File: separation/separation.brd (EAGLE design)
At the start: 71.1 x 26.7 mm, 9 parts, among them IC1 L7805ACV

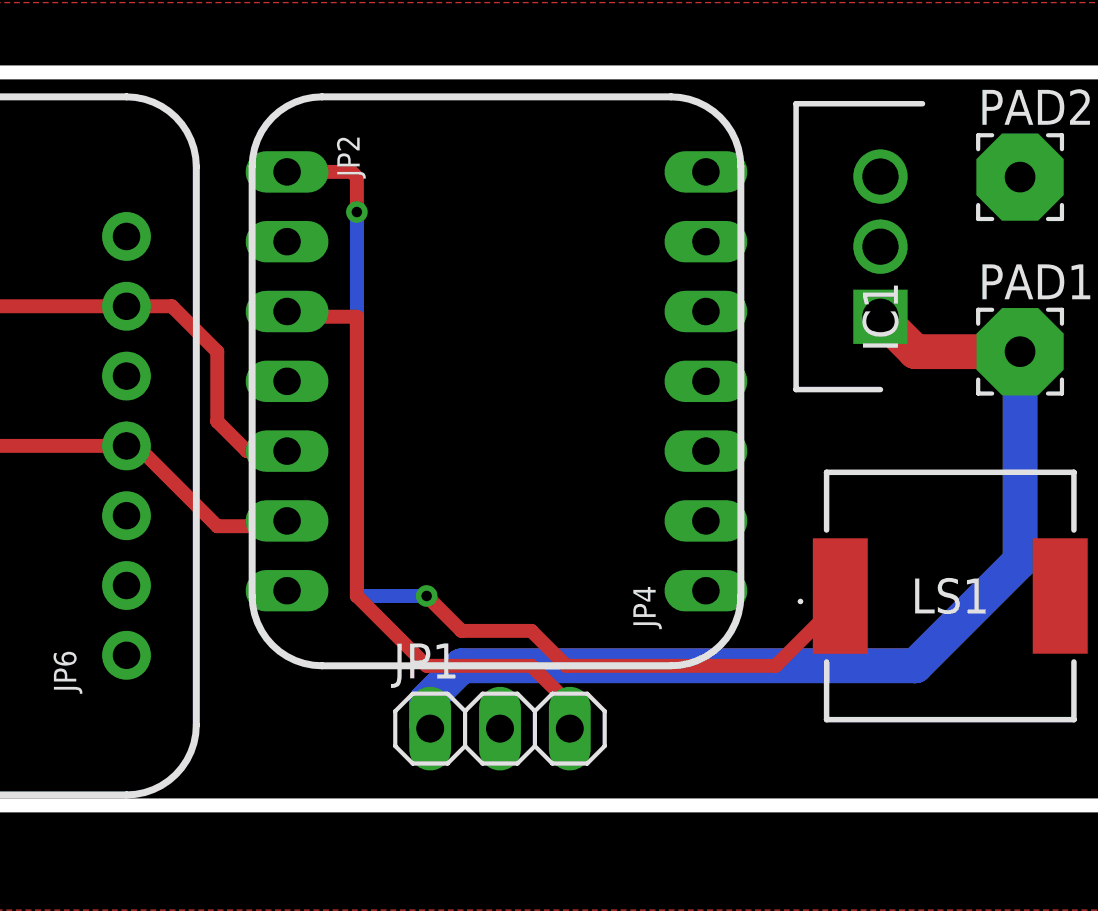
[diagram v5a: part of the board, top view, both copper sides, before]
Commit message: tweak rp2040 tstop
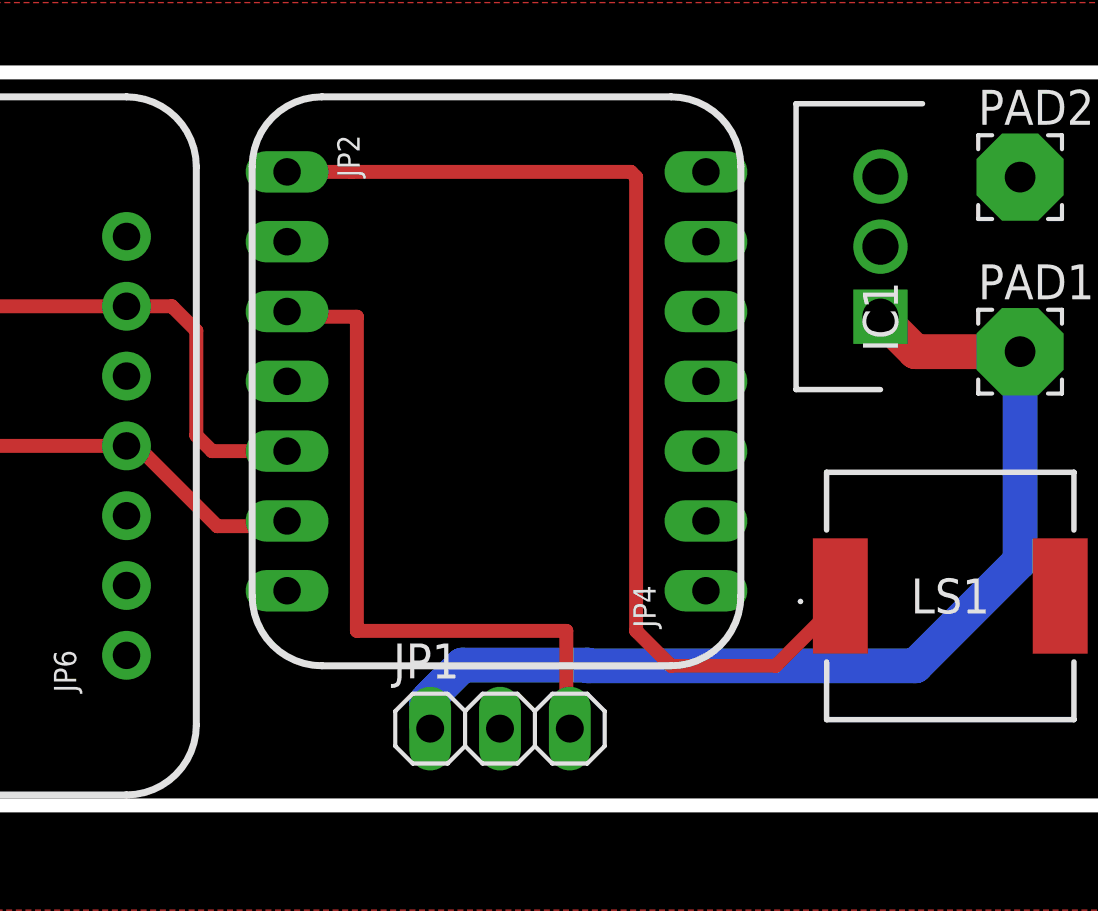
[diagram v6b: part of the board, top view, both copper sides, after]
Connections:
- removed net SDO/ADR_2: JP6.5
- net GND: now also JP6.5
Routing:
- net SERVO: track 23.0 -> 25.3 mm
- net VBAT: track 38.0 -> 39.0 mm
- net SDA: track 28.2 -> 29.0 mm
- net BUZZ: track 37.7 -> 38.4 mm, vias 2 -> 0
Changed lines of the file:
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@@
 <wire x1="133.35" y1="77.851" x2="135.89" y2="75.311" width="0.254" layer="21" curve="-90"/>
 <text x="111.4298" y="61.0108" size="1.016" layer="21" font="vector" ratio="12" rot="R180" align="center"></text>
-<wire x1="119.38" y1="75.184" x2="117.348" y2="75.184" width="1.524" layer="29"/>
-<wire x1="119.38" y1="72.517" x2="117.348" y2="72.517" width="1.524" layer="29"/>
+<wire x1="119.634" y1="75.057" x2="117.602" y2="75.057" width="1.524" layer="29"/>
+<wire x1="119.634" y1="72.517" x2="117.602" y2="72.517" width="1.524" layer="29"/>
 <wire x1="119.38" y1="69.977" x2="119.253" y2="70.104" width="1.524" layer="29"/>
 <wire x1="119.38" y1="65.024" x2="119.253" y2="64.897" width="1.524" layer="29"/>
 <wire x1="119.253" y1="64.897" x2="117.602" y2="64.897" width="1.524" layer="29"/>
 <wire x1="119.38" y1="69.977" x2="117.602" y2="69.977" width="1.524" layer="29"/>
-<wire x1="119.38" y1="67.437" x2="119.253" y2="67.31" width="1.524" layer="29"/>
-<wire x1="119.253" y1="67.31" x2="117.602" y2="67.31" width="1.524" layer="29"/>
+<wire x1="119.38" y1="67.691" x2="119.253" y2="67.564" width="1.524" layer="29"/>
+<wire x1="119.253" y1="67.564" x2="117.602" y2="67.564" width="1.524" layer="29"/>
 <wire x1="119.38" y1="62.357" x2="117.602" y2="62.357" width="1.524" layer="29"/>
 <wire x1="119.38" y1="59.817" x2="117.602" y2="59.817" width="1.524" layer="29"/>
@@
 <vertex x="153.67" y="81.28"/>
 </polygon>
-<wire x1="140.97" y1="72.4" x2="146.05" y2="74.93" width="0" layer="19" extent="1-1"/>
-<wire x1="134.62" y1="72.5805" x2="140.97" y2="72.4" width="0" layer="19" extent="1-1"/>
-<wire x1="147.51" y1="59.69" x2="140.97" y2="72.4" width="0" layer="19" extent="1-1"/>
-<wire x1="127.127" y1="54.864" x2="134.62" y2="72.5805" width="0" layer="19" extent="1-1"/>
-<wire x1="113.538" y1="62.611" x2="127.127" y2="54.864" width="0" layer="19" extent="1-1"/>
-<wire x1="94.869" y1="62.738" x2="113.538" y2="62.611" width="0" layer="19" extent="1-1"/>
+<contactref element="JP6" pad="5"/>
+<wire x1="113.538" y1="62.611" x2="113.538" y2="67.691" width="0" layer="19" extent="1-1"/>
 </signal>
 <signal name="A1">
@@
 <wire x1="119.5705" y1="69.85" x2="119.38" y2="70.0405" width="0.508" layer="1"/>
 <wire x1="129.667" y1="54.864" x2="129.54" y2="54.991" width="0.508" layer="1"/>
-<wire x1="129.54" y1="54.991" x2="129.54" y2="55.88" width="0.508" layer="1"/>
-<wire x1="129.54" y1="55.88" x2="128.27" y2="57.15" width="0.508" layer="1"/>
-<wire x1="128.27" y1="57.15" x2="124.46" y2="57.15" width="0.508" layer="1"/>
-<wire x1="124.46" y1="57.15" x2="121.92" y2="59.69" width="0.508" layer="1"/>
+<wire x1="129.54" y1="58.42" x2="121.92" y2="58.42" width="0.508" layer="1"/>
 <wire x1="121.92" y1="69.85" x2="119.5705" y2="69.85" width="0.508" layer="1"/>
-<wire x1="121.92" y1="59.69" x2="121.92" y2="69.85" width="0.508" layer="1"/>
+<wire x1="129.54" y1="54.991" x2="129.54" y2="58.42" width="0.508" layer="1"/>
+<wire x1="121.92" y1="58.42" x2="121.92" y2="69.85" width="0.508" layer="1"/>
 </signal>
 <signal name="A3">
@@
 <contactref element="JP3" pad="6"/>
 <contactref element="JP6" pad="6"/>
-<wire x1="119.38" y1="64.9605" x2="117.9195" y2="64.9605" width="0.508" layer="1"/>
-<wire x1="117.9195" y1="64.9605" x2="116.84" y2="66.04" width="0.508" layer="1"/>
-<wire x1="116.84" y1="66.04" x2="116.84" y2="68.58" width="0.508" layer="1"/>
-<wire x1="116.84" y1="68.58" x2="115.189" y2="70.231" width="0.508" layer="1"/>
+<wire x1="119.38" y1="64.9605" x2="116.6495" y2="64.9605" width="0.508" layer="1"/>
+<wire x1="116.6495" y1="64.9605" x2="116.078" y2="65.532" width="0.508" layer="1"/>
+<wire x1="116.078" y1="65.532" x2="116.078" y2="69.342" width="0.508" layer="1"/>
+<wire x1="116.078" y1="69.342" x2="115.189" y2="70.231" width="0.508" layer="1"/>
 <wire x1="115.189" y1="70.231" x2="113.538" y2="70.231" width="0.508" layer="1"/>
 <wire x1="113.538" y1="70.231" x2="94.996" y2="70.231" width="0.508" layer="1"/>
@@
 <vertex x="72.39" y="45.72"/>
 </polygon>
-<wire x1="134.62" y1="75.1205" x2="140.97" y2="74.95" width="0" layer="19" extent="1-1"/>
-<wire x1="113.538" y1="57.531" x2="134.62" y2="75.1205" width="0" layer="19" extent="1-1"/>
-<wire x1="94.869" y1="57.658" x2="113.538" y2="57.531" width="0" layer="19" extent="1-1"/>
 </signal>
 <signal name="PB22/I6/SERCOM5.1">
@@
 <signal name="SDO/ADR">
 <contactref element="JP3" pad="5"/>
-</signal>
-<signal name="SDO/ADR_2">
-<contactref element="JP6" pad="5"/>
 </signal>
 <signal name="VBAT">
@@
 <wire x1="124.587" y1="54.864" x2="124.46" y2="54.991" width="1.27" layer="16"/>
 <wire x1="124.46" y1="54.991" x2="124.46" y2="55.88" width="1.27" layer="16"/>
-<wire x1="124.46" y1="55.88" x2="125.73" y2="57.15" width="1.27" layer="16"/>
-<wire x1="125.73" y1="57.15" x2="142.24" y2="57.15" width="1.27" layer="16"/>
 <wire x1="142.24" y1="57.15" x2="146.05" y2="60.96" width="1.27" layer="16"/>
 <wire x1="146.05" y1="60.96" x2="146.05" y2="68.58" width="1.27" layer="16"/>
+<wire x1="124.587" y1="54.864" x2="124.587" y2="56.007" width="1.27" layer="16"/>
+<wire x1="130.3087875" y1="57.1754" x2="130.3341875" y2="57.15" width="1.27" layer="16"/>
+<wire x1="125.7554" y1="57.1754" x2="130.3087875" y2="57.1754" width="1.27" layer="16"/>
+<wire x1="124.587" y1="56.007" x2="125.7554" y2="57.1754" width="1.27" layer="16"/>
+<wire x1="130.3341875" y1="57.15" x2="142.24" y2="57.15" width="1.27" layer="16"/>
 </signal>
 <signal name="BUZZ">
@@
 <contactref element="JP2" pad="1"/>
 <wire x1="119.38" y1="75.1205" x2="121.7295" y2="75.1205" width="0.508" layer="1"/>
-<wire x1="121.7295" y1="75.1205" x2="121.92" y2="74.93" width="0.508" layer="1"/>
-<wire x1="121.92" y1="74.93" x2="121.92" y2="73.66" width="0.508" layer="1"/>
-<via x="121.92" y="73.66" extent="1-16" drill="0.381"/>
-<via x="124.46" y="59.69" extent="1-16" drill="0.381"/>
-<wire x1="121.92" y1="73.66" x2="121.92" y2="59.69" width="0.508" layer="16"/>
-<wire x1="124.46" y1="59.69" x2="121.92" y2="59.69" width="0.508" layer="16"/>
-<wire x1="124.46" y1="59.69" x2="125.73" y2="58.42" width="0.508" layer="1"/>
-<wire x1="125.73" y1="58.42" x2="128.27" y2="58.42" width="0.508" layer="1"/>
-<wire x1="128.27" y1="58.42" x2="129.54" y2="57.15" width="0.508" layer="1"/>
+<wire x1="139.51" y1="59.5" x2="139.51" y2="59.69" width="0.508" layer="1"/>
+<wire x1="133.35" y1="57.15" x2="132.08" y2="58.42" width="0.508" layer="1"/>
 <wire x1="137.16" y1="57.15" x2="139.51" y2="59.5" width="0.508" layer="1"/>
-<wire x1="139.51" y1="59.5" x2="139.51" y2="59.69" width="0.508" layer="1"/>
-<wire x1="129.54" y1="57.15" x2="137.16" y2="57.15" width="0.508" layer="1"/>
+<wire x1="133.35" y1="57.15" x2="137.16" y2="57.15" width="0.508" layer="1"/>
+<wire x1="132.08" y1="74.93" x2="131.8895" y2="75.1205" width="0.508" layer="1"/>
+<wire x1="131.8895" y1="75.1205" x2="121.7295" y2="75.1205" width="0.508" layer="1"/>
+<wire x1="132.08" y1="58.42" x2="132.08" y2="74.93" width="0.508" layer="1"/>
 </signal>
 </signals>

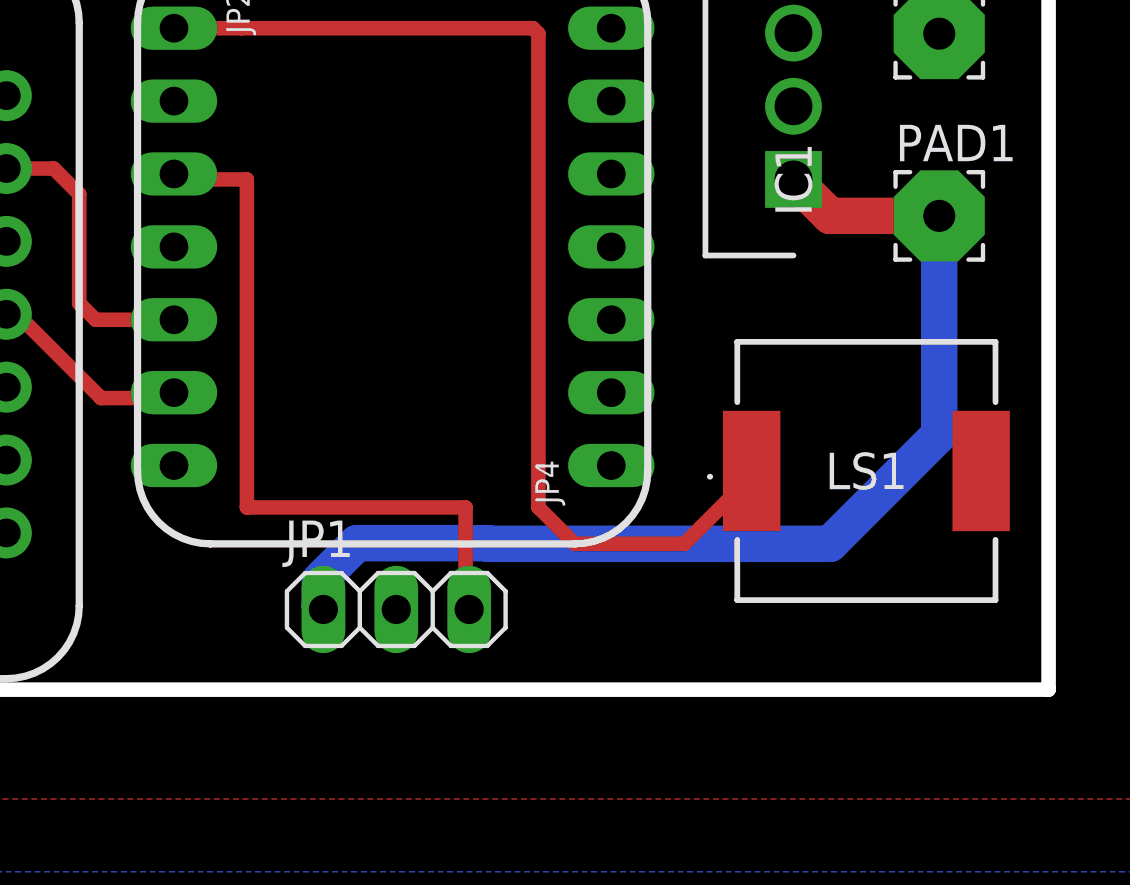
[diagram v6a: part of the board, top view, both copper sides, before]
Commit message: flip servo connector for better routing
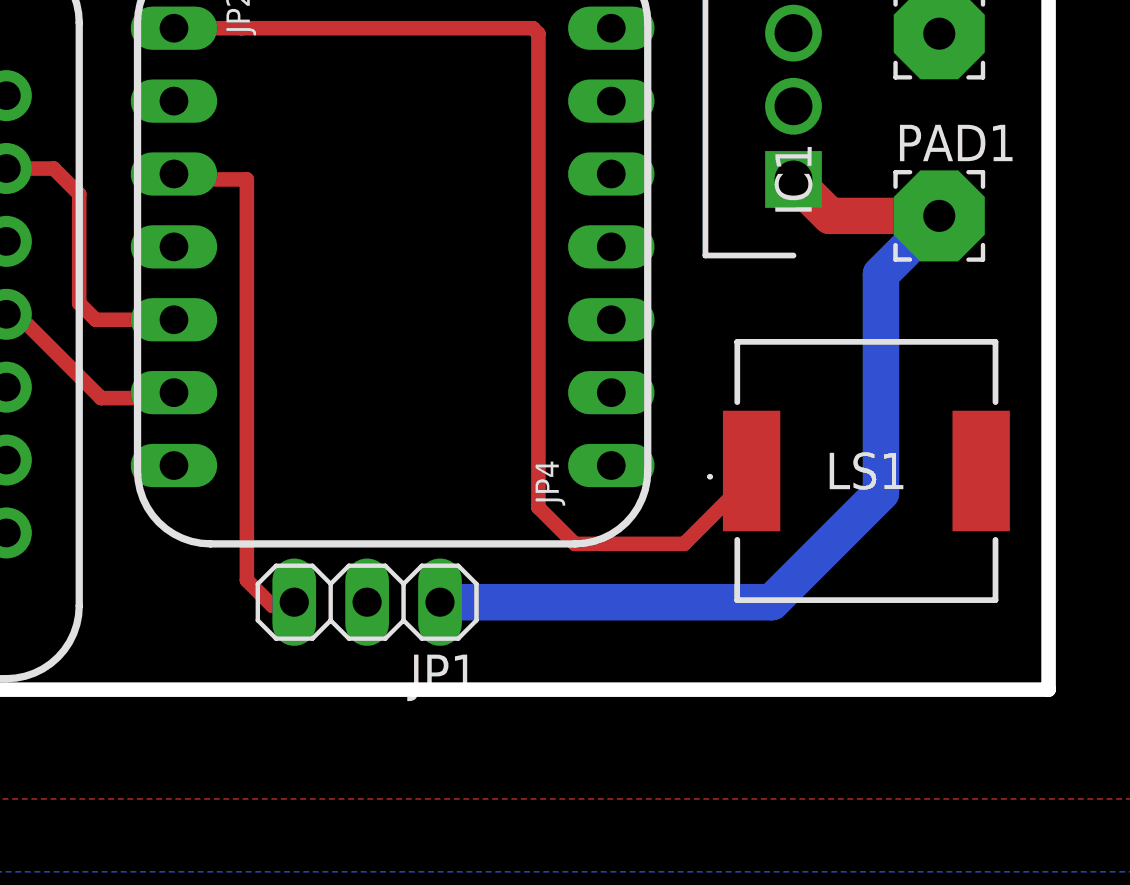
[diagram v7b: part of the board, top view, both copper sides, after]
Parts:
- moved JP1 1.05 mm to (126.1, 55.1), turned to 180 degrees
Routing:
- net SERVO: track 25.3 -> 18.9 mm
- net VBAT: track 39.0 -> 33.0 mm
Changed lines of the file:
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@@
 <attribute name="VALUE" x="143.51" y="59.69" size="1.27" layer="27" align="center"/>
 </element>
-<element name="JP1" library="pinhead" library_urn="urn:adsk.eagle:library:325" package="1X03" package3d_urn="urn:adsk.eagle:package:22458/2" value="" x="127.127" y="54.864" smashed="yes">
-<attribute name="NAME" x="123.2408" y="56.6928" size="1.27" layer="25" ratio="10"/>
-<attribute name="POPULARITY" value="92" x="127.127" y="54.864" size="1.778" layer="27" font="vector" ratio="15" display="off"/>
-<attribute name="VALUE" x="123.317" y="51.689" size="1.27" layer="27"/>
+<element name="JP1" library="pinhead" library_urn="urn:adsk.eagle:library:325" package="1X03" package3d_urn="urn:adsk.eagle:package:22458/2" value="" x="126.111" y="55.118" smashed="yes" rot="R180">
+<attribute name="NAME" x="129.9972" y="53.2892" size="1.27" layer="25" ratio="10" rot="R180"/>
+<attribute name="POPULARITY" value="92" x="126.111" y="55.118" size="1.778" layer="27" font="vector" ratio="15" rot="R180" display="off"/>
+<attribute name="VALUE" x="129.921" y="58.293" size="1.27" layer="27" rot="R180"/>
 </element>
 <element name="PAD1" library="wirepad" library_urn="urn:adsk.eagle:library:412" package="3,17/1,1" package3d_urn="urn:adsk.eagle:package:30832/1" value="WIREPAD3,17/1,1" x="146.05" y="68.58" smashed="yes">
@@
 <contactref element="JP1" pad="3"/>
 <wire x1="119.5705" y1="69.85" x2="119.38" y2="70.0405" width="0.508" layer="1"/>
-<wire x1="129.667" y1="54.864" x2="129.54" y2="54.991" width="0.508" layer="1"/>
-<wire x1="129.54" y1="58.42" x2="121.92" y2="58.42" width="0.508" layer="1"/>
-<wire x1="121.92" y1="69.85" x2="119.5705" y2="69.85" width="0.508" layer="1"/>
-<wire x1="129.54" y1="54.991" x2="129.54" y2="58.42" width="0.508" layer="1"/>
-<wire x1="121.92" y1="58.42" x2="121.92" y2="69.85" width="0.508" layer="1"/>
+<wire x1="123.698" y1="54.991" x2="123.571" y2="55.118" width="0.508" layer="1"/>
+<wire x1="119.5705" y1="69.85" x2="121.92" y2="69.85" width="0.508" layer="1"/>
+<wire x1="121.92" y1="69.85" x2="121.92" y2="55.88" width="0.508" layer="1"/>
+<wire x1="121.92" y1="55.88" x2="122.809" y2="54.991" width="0.508" layer="1"/>
+<wire x1="122.809" y1="54.991" x2="123.698" y2="54.991" width="0.508" layer="1"/>
 </signal>
 <signal name="A3">
@@
 <wire x1="146.05" y1="68.58" x2="142.24" y2="68.58" width="1.27" layer="1"/>
 <wire x1="142.24" y1="68.58" x2="140.97" y2="69.85" width="1.27" layer="1"/>
-<wire x1="124.587" y1="54.864" x2="124.46" y2="54.991" width="1.27" layer="16"/>
-<wire x1="124.46" y1="54.991" x2="124.46" y2="55.88" width="1.27" layer="16"/>
-<wire x1="142.24" y1="57.15" x2="146.05" y2="60.96" width="1.27" layer="16"/>
-<wire x1="146.05" y1="60.96" x2="146.05" y2="68.58" width="1.27" layer="16"/>
-<wire x1="124.587" y1="54.864" x2="124.587" y2="56.007" width="1.27" layer="16"/>
-<wire x1="130.3087875" y1="57.1754" x2="130.3341875" y2="57.15" width="1.27" layer="16"/>
-<wire x1="125.7554" y1="57.1754" x2="130.3087875" y2="57.1754" width="1.27" layer="16"/>
-<wire x1="124.587" y1="56.007" x2="125.7554" y2="57.1754" width="1.27" layer="16"/>
-<wire x1="130.3341875" y1="57.15" x2="142.24" y2="57.15" width="1.27" layer="16"/>
+<wire x1="146.05" y1="68.58" x2="144.018" y2="66.548" width="1.27" layer="16"/>
+<wire x1="144.018" y1="66.548" x2="144.018" y2="58.928" width="1.27" layer="16"/>
+<wire x1="144.018" y1="58.928" x2="140.208" y2="55.118" width="1.27" layer="16"/>
+<wire x1="140.208" y1="55.118" x2="128.651" y2="55.118" width="1.27" layer="16"/>
 </signal>
 <signal name="BUZZ">
